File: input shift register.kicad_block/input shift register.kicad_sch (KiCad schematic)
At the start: 10 parts, among them U1 74HC165

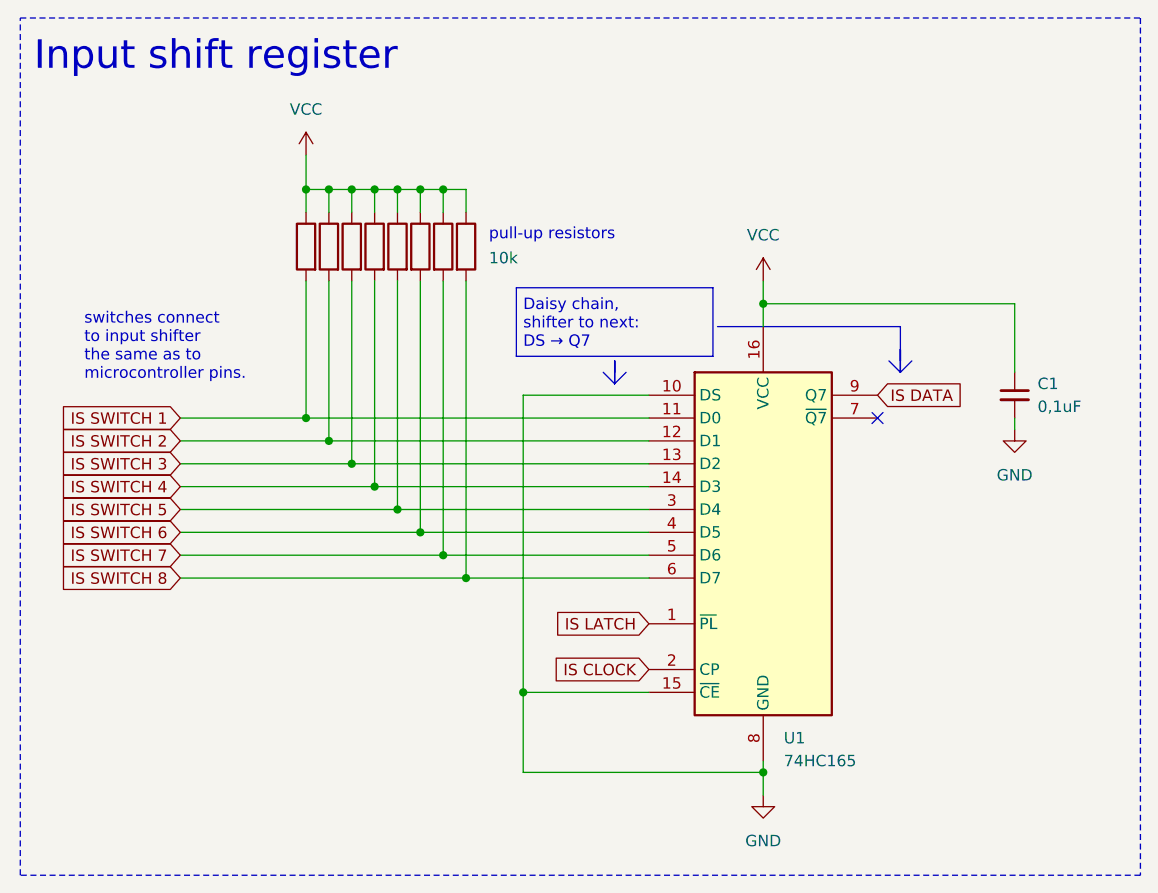
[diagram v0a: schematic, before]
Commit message: added info about daisy chaining to input shift register design block.
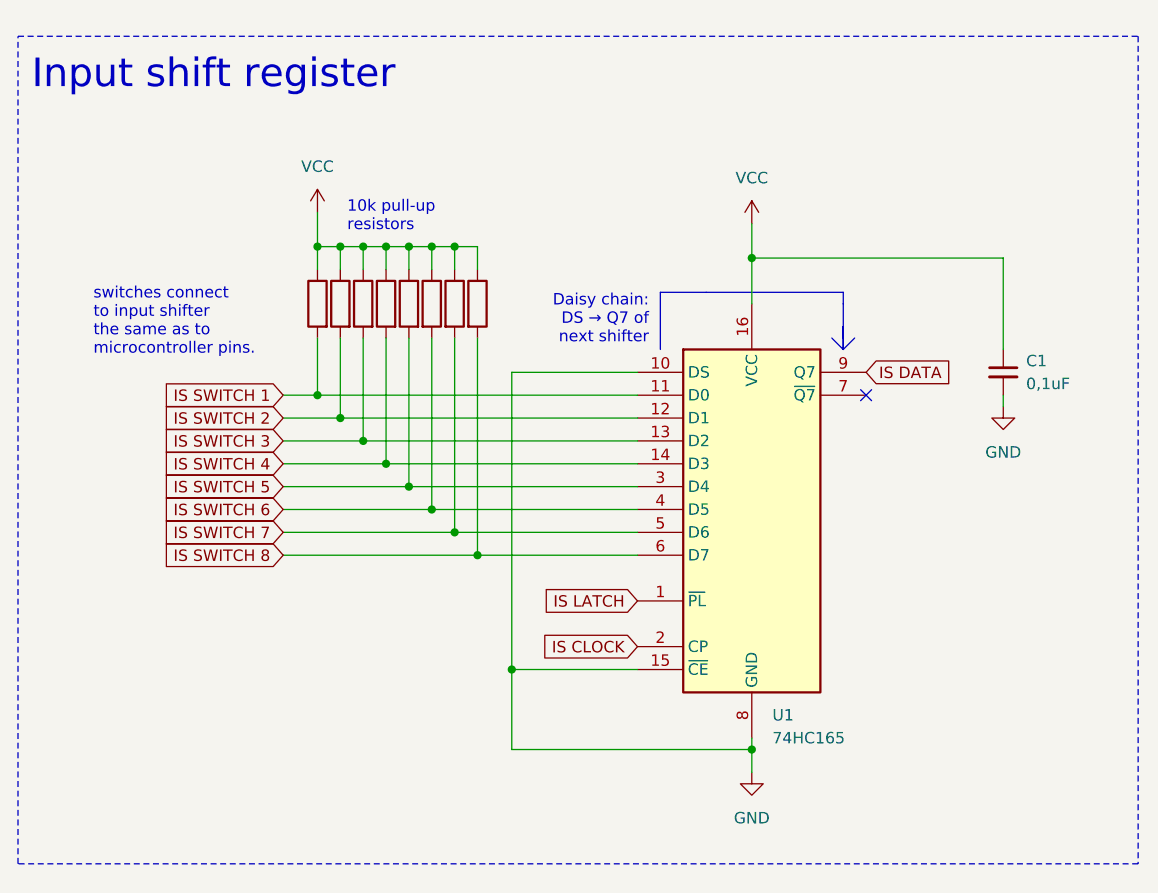
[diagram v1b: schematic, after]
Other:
- note added: "10k pull-up resistors"
- note added: "Daisy chain: DS → Q7 of next shifter"
- note removed: "Daisy chain, shifter to next: DS → Q7"
- note removed: "pull-up resistors"
- moved on the sheet: C1, U1
